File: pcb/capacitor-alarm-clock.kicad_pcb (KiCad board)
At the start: 2 copper layers, 62.3 x 64.3 mm, 93 parts

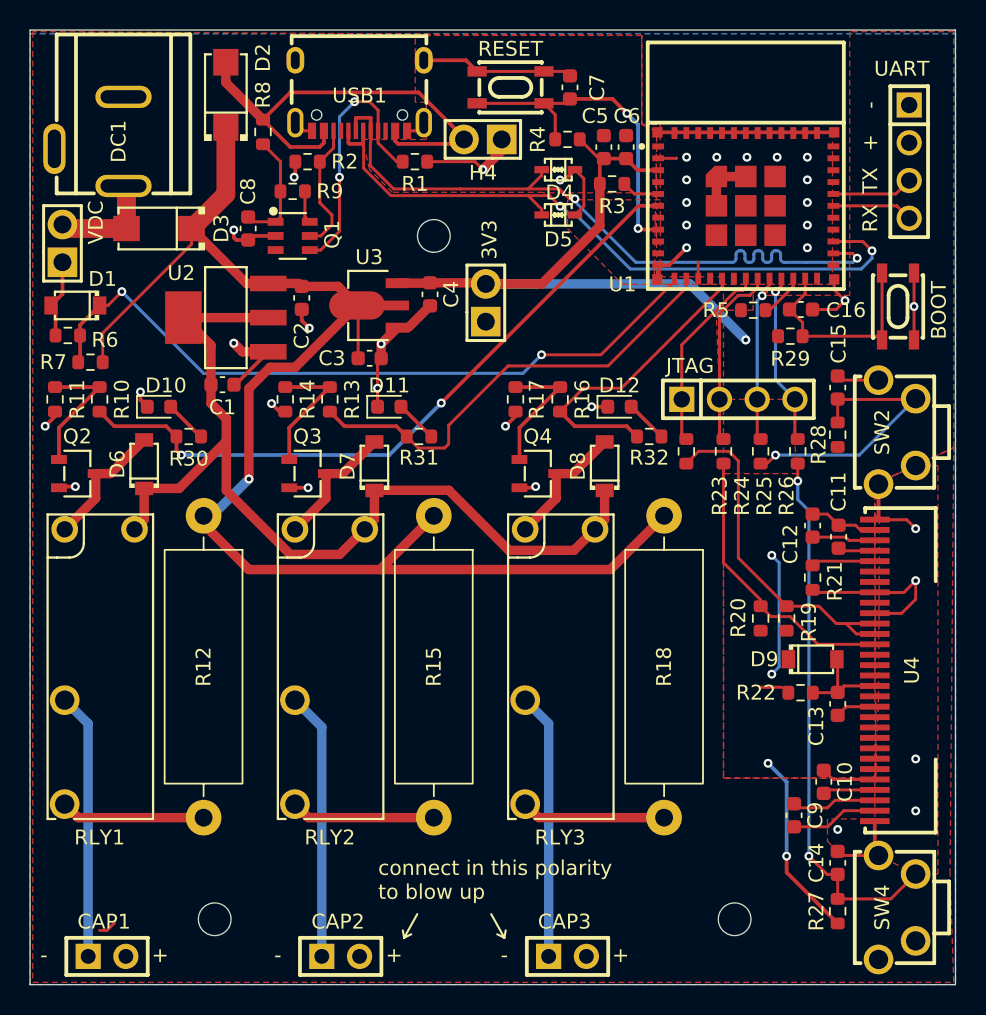
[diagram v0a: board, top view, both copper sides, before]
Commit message: Connected reset pin to gpio2
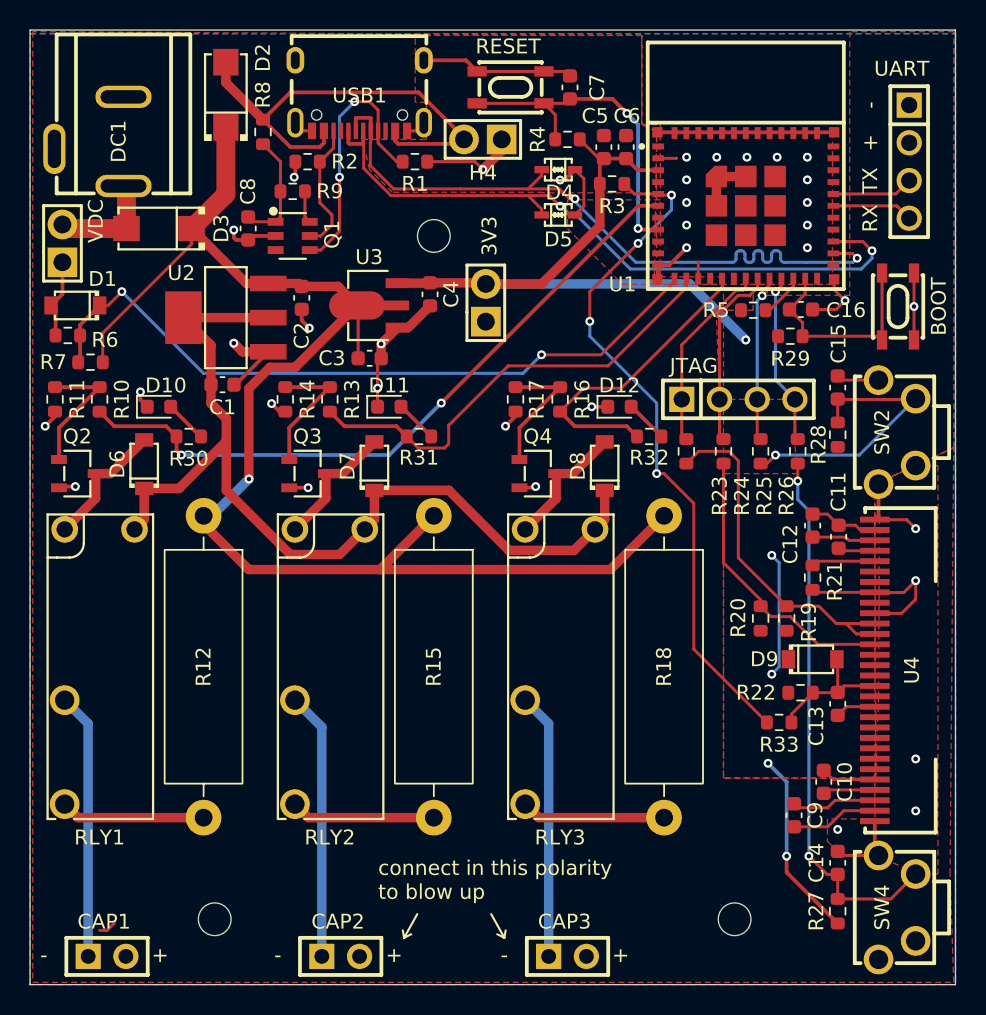
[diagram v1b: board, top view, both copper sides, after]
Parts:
- added R33: 1K, Resistor_SMD:R_0603_1608Metric, F.Cu at (70.8, 71.2)
- renumbered 3V3 to H1, REF** to H10, REF** to H11, VDC to H2, UART to H3, JTAG to H5, REF** to H9, RESET to SW1, BOOT to SW3
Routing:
- net /ESP32/IO2: track 2.55 -> 46.5 mm, vias 0 -> 4
- net /Display/SSD_RST: track 6.61 -> 9.21 mm
- net +3V3: track 68.1 -> 66.6 mm
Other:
- board text added: "3V3"
- board text added: "BOOT"
- board text added: "JTAG"
- board text added: "RESET"
- board text added: "UART"
- board text added: "VDC"

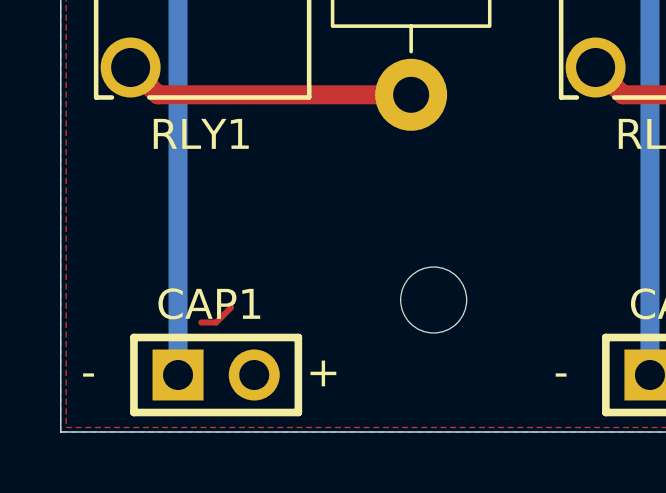
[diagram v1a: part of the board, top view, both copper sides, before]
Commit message: Add next slot and one-day disable
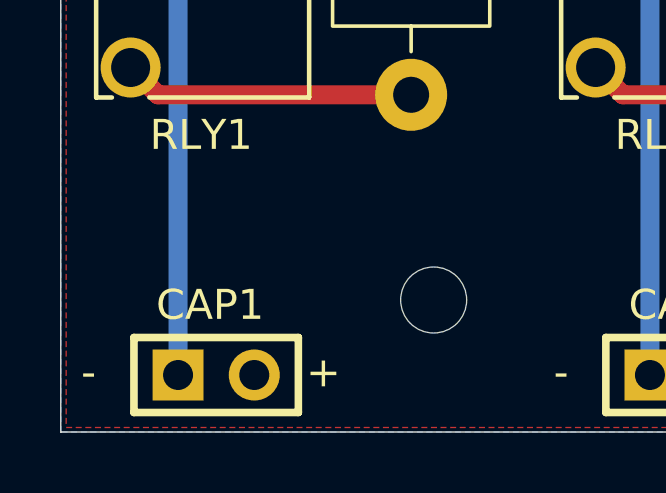
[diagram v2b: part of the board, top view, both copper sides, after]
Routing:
- net (no net): track 1.21 -> 0.00 mm
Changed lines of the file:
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@@
-	)
-	(segment
-		(start 25 85.25)
-		(end 25.5 85.25)
-		(width 0.2)
-		(layer "F.Cu")
-		(net 0)
-	)
-	(segment
-		(start 25.5 85.25)
-		(end 26 84.75)
-		(width 0.2)
-		(layer "F.Cu")
-		(net 0)
 	)
 	(segment
